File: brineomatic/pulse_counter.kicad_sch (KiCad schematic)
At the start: 6 parts

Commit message: worked on bom for rev b prototype run
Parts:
- C2: LCSC C107149 -> (none)
- R7: LCSC C114526 -> (none)
- R8: LCSC C114561 -> (none)
- R9: LCSC C60816 -> (none)
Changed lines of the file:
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@@
 			)
 		)
-		(property "LCSC" "C60816"
+		(property "LCSC" ""
 			(at 124.46 104.14 0)
 			(effects
@@
 			)
 		)
-		(property "LCSC" "C114526"
+		(property "LCSC" ""
 			(at 111.76 100.33 0)
 			(effects
@@
 			)
 		)
-		(property "LCSC" "C107149"
+		(property "LCSC" ""
 			(at 130.81 107.95 0)
 			(effects
@@
 			)
 		)
-		(property "LCSC" "C114561"
+		(property "LCSC" ""
 			(at 111.76 107.95 0)
 			(effects

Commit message: updated jlc parts rotations and placement offsets
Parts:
- J2: Rotation Offset (none) -> 180
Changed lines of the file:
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@@
+			)
+		)
+		(property "Rotation Offset" "180"
+			(at 100.33 104.14 0)
+			(effects
+				(font
+					(size 1.27 1.27)
+				)
+				(hide yes)
 			)
 		)

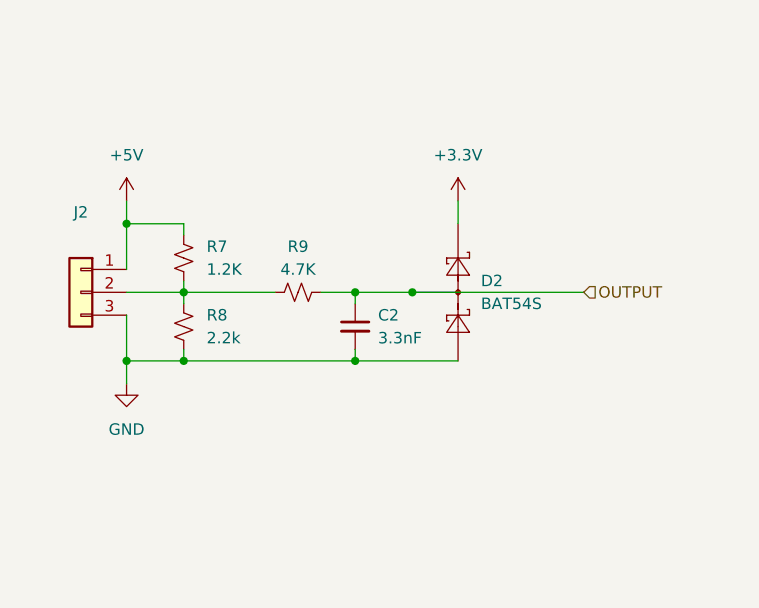
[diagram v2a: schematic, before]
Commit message: added qwiic i2c connector
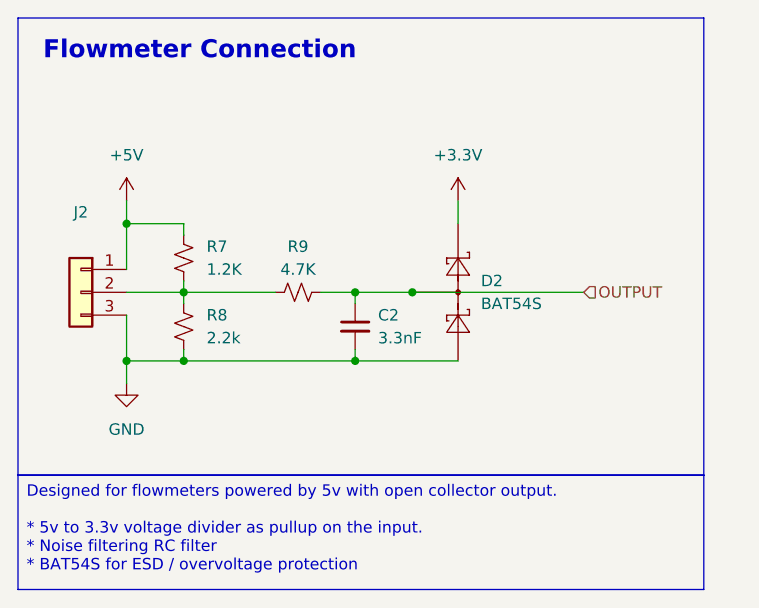
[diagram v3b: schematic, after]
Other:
- note added: "Flowmeter Connection"
- title: (none) -> https://github.com/hoeken/brineomatic
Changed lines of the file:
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@@
 	(generator_version "9.0")
 	(paper "A4")
+	(title_block
+		(title "https://github.com/hoeken/brineomatic")
+		(date "2025-08-28")
+		(rev "B")
+	)
+	(rectangle
+		(start 93.345 73.66)
+		(end 169.545 124.46)
+		(stroke
+			(width 0)
+			(type default)
+		)
+		(fill
+			(type none)
+		)
+	)
+	(text "Flowmeter Connection"
+		(exclude_from_sim no)
+		(at 96.139 77.343 0)
+		(effects
+			(font
+				(size 2 2)
+				(thickness 0.4)
+				(bold yes)
+			)
+			(justify left)
+		)
+	)
+	(text_box "Designed for flowmeters powered by 5v with open collector output.\n\n* 5v to 3.3v voltage divider as pullup on the input.\n* Noise filtering RC filter\n* BAT54S for ESD / overvoltage protection"
+		(exclude_from_sim no)
+		(at 93.345 124.46 0)
+		(size 76.2 12.7)
+		(margins 0.9525 0.9525 0.9525 0.9525)
+		(stroke
+			(width 0)
+			(type solid)
+		)
+		(fill
+			(type none)
+		)
+		(effects
+			(font
+				(size 1.27 1.27)
+			)
+			(justify left top)
+		)
+	)
 	(junction
 		(at 111.76 111.76)

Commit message: added pullup resistor to adc alert
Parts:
- renumbered J2 to J3, R7 to R5, R8 to R6, R9 to R7
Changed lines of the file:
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@@
 		(dnp no)
 		(fields_autoplaced yes)
-		(property "Reference" "#PWR011"
+		(property "Reference" "#PWR013"
 			(at 105.41 120.65 0)
 			(effects
@@
 			(project "brineomatic"
 				(path "/96477ae2-ef08-48f3-8dd4-fe4478541f68/afb25a63-7dc0-4ba4-a0ca-4f0b83c59f3b"
-					(reference "#PWR011")
-					(unit 1)
-				)
-				(path "/96477ae2-ef08-48f3-8dd4-fe4478541f68/c28d9395-3f2f-46b5-bdab-c14b6c7c5c4b"
-					(reference "#PWR031")
+					(reference "#PWR013")
+					(unit 1)
+				)
+				(path "/96477ae2-ef08-48f3-8dd4-fe4478541f68/c28d9395-3f2f-46b5-bdab-c14b6c7c5c4b"
+					(reference "#PWR033")
 					(unit 1)
 				)
@@
 		(dnp no)
 		(fields_autoplaced yes)
-		(property "Reference" "#PWR012"
+		(property "Reference" "#PWR014"
 			(at 142.24 97.79 0)
 			(effects
@@
 			(project "brineomatic"
 				(path "/96477ae2-ef08-48f3-8dd4-fe4478541f68/afb25a63-7dc0-4ba4-a0ca-4f0b83c59f3b"
-					(reference "#PWR012")
-					(unit 1)
-				)
-				(path "/96477ae2-ef08-48f3-8dd4-fe4478541f68/c28d9395-3f2f-46b5-bdab-c14b6c7c5c4b"
-					(reference "#PWR032")
+					(reference "#PWR014")
+					(unit 1)
+				)
+				(path "/96477ae2-ef08-48f3-8dd4-fe4478541f68/c28d9395-3f2f-46b5-bdab-c14b6c7c5c4b"
+					(reference "#PWR034")
 					(unit 1)
 				)
@@
 		(dnp no)
 		(fields_autoplaced yes)
-		(property "Reference" "#PWR010"
+		(property "Reference" "#PWR012"
 			(at 105.41 97.79 0)
 			(effects
@@
 			(project "brineomatic"
 				(path "/96477ae2-ef08-48f3-8dd4-fe4478541f68/afb25a63-7dc0-4ba4-a0ca-4f0b83c59f3b"
-					(reference "#PWR010")
-					(unit 1)
-				)
-				(path "/96477ae2-ef08-48f3-8dd4-fe4478541f68/c28d9395-3f2f-46b5-bdab-c14b6c7c5c4b"
-					(reference "#PWR030")
+					(reference "#PWR012")
+					(unit 1)
+				)
+				(path "/96477ae2-ef08-48f3-8dd4-fe4478541f68/c28d9395-3f2f-46b5-bdab-c14b6c7c5c4b"
+					(reference "#PWR032")
 					(unit 1)
 				)
@@
 		(on_board yes)
 		(dnp no)
-		(property "Reference" "R9"
+		(property "Reference" "R7"
 			(at 124.46 99.06 90)
 			(effects
@@
 			(project "brineomatic"
 				(path "/96477ae2-ef08-48f3-8dd4-fe4478541f68/afb25a63-7dc0-4ba4-a0ca-4f0b83c59f3b"
-					(reference "R9")
+					(reference "R7")
 					(unit 1)
 				)
@@
 		(dnp no)
 		(fields_autoplaced yes)
-		(property "Reference" "J2"
+		(property "Reference" "J3"
 			(at 100.33 95.25 0)
 			(effects
@@
 			(project "brineomatic"
 				(path "/96477ae2-ef08-48f3-8dd4-fe4478541f68/afb25a63-7dc0-4ba4-a0ca-4f0b83c59f3b"
-					(reference "J2")
-					(unit 1)
-				)
-				(path "/96477ae2-ef08-48f3-8dd4-fe4478541f68/c28d9395-3f2f-46b5-bdab-c14b6c7c5c4b"
-					(reference "J10")
+					(reference "J3")
+					(unit 1)
+				)
+				(path "/96477ae2-ef08-48f3-8dd4-fe4478541f68/c28d9395-3f2f-46b5-bdab-c14b6c7c5c4b"
+					(reference "J11")
 					(unit 1)
 				)
@@
 		(dnp no)
 		(fields_autoplaced yes)
-		(property "Reference" "R7"
+		(property "Reference" "R5"
 			(at 114.3 99.0599 0)
 			(effects
@@
 			(project "brineomatic"
 				(path "/96477ae2-ef08-48f3-8dd4-fe4478541f68/afb25a63-7dc0-4ba4-a0ca-4f0b83c59f3b"
-					(reference "R7")
+					(reference "R5")
 					(unit 1)
 				)
@@
 				)
 				(path "/96477ae2-ef08-48f3-8dd4-fe4478541f68/c28d9395-3f2f-46b5-bdab-c14b6c7c5c4b"
-					(reference "C13")
+					(reference "C14")
 					(unit 1)
 				)
@@
 		(dnp no)
 		(fields_autoplaced yes)
-		(property "Reference" "R8"
+		(property "Reference" "R6"
 			(at 114.3 106.6799 0)
 			(effects
@@
 			(project "brineomatic"
 				(path "/96477ae2-ef08-48f3-8dd4-fe4478541f68/afb25a63-7dc0-4ba4-a0ca-4f0b83c59f3b"
-					(reference "R8")
-					(unit 1)
-				)
+					(reference "R6")
+					(unit 1)
+				)

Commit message: 5v power supply is sorted.
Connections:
- net +5V renamed 5V_TRUE
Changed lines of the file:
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@@
+		)
+	)
+	(global_label "5V_TRUE"
+		(shape input)
+		(at 105.41 93.98 90)
+		(fields_autoplaced yes)
+		(effects
+			(font
+				(size 1.27 1.27)
+			)
+			(justify left)
+		)
+		(property "Intersheetrefs" "${INTERSHEET_REFS}"
+			(at 105.41 83.012 90)
+			(effects
+				(font
+					(size 1.27 1.27)
+				)
+				(justify left)
+				(hide yes)
+			)
 		)
 	)
@@
 					(unit 1)
 				)
-			)
-		)
-	)
-	(symbol
-		(lib_id "power:+5V")
-		(at 105.41 93.98 0)
-		(unit 1)
-		(exclude_from_sim no)
-		(in_bom yes)
-		(on_board yes)
-		(dnp no)
-		(fields_autoplaced yes)
-		(property "Reference" "#PWR012"
-			(at 105.41 97.79 0)
-			(effects
-				(font
-					(size 1.27 1.27)
-				)
-				(hide yes)
-			)
-		)
-		(property "Value" "+5V"
-			(at 105.41 88.9 0)
-			(effects
-				(font
-					(size 1.27 1.27)
-				)
-			)
-		)
-		(property "Footprint" ""
-			(at 105.41 93.98 0)
-			(effects
-				(font
-					(size 1.27 1.27)
-				)
-				(hide yes)
-			)
-		)
-		(property "Datasheet" ""
-			(at 105.41 93.98 0)
-			(effects
-				(font
-					(size 1.27 1.27)
-				)
-				(hide yes)
-			)
-		)
-		(property "Description" "Power symbol creates a global label with name \"+5V\""
-			(at 105.41 93.98 0)
-			(effects
-				(font
-					(size 1.27 1.27)
-				)
-				(hide yes)
-			)
-		)
-		(pin "1"
-		)
-		(instances
-			(project "brineomatic"
-				(path "/96477ae2-ef08-48f3-8dd4-fe4478541f68/afb25a63-7dc0-4ba4-a0ca-4f0b83c59f3b"
-					(reference "#PWR012")
-					(unit 1)
-				)
-				(path "/96477ae2-ef08-48f3-8dd4-fe4478541f68/c28d9395-3f2f-46b5-bdab-c14b6c7c5c4b"
-					(reference "#PWR032")
-					(unit 1)
-				)

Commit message: stacked tds, removed stepper vref, pulled in esp32-s3 schematic, added extra relay output
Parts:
- renumbered J3 to J4
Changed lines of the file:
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@@
 		(dnp no)
 		(fields_autoplaced yes)
-		(property "Reference" "#PWR013"
+		(property "Reference" "#PWR014"
 			(at 105.41 120.65 0)
 			(effects
@@
 			(project "brineomatic"
 				(path "/96477ae2-ef08-48f3-8dd4-fe4478541f68/afb25a63-7dc0-4ba4-a0ca-4f0b83c59f3b"
-					(reference "#PWR013")
+					(reference "#PWR014")
 					(unit 1)
 				)
 				(path "/96477ae2-ef08-48f3-8dd4-fe4478541f68/c28d9395-3f2f-46b5-bdab-c14b6c7c5c4b"
-					(reference "#PWR033")
+					(reference "#PWR032")
 					(unit 1)
 				)
@@
 		(dnp no)
 		(fields_autoplaced yes)
-		(property "Reference" "#PWR014"
+		(property "Reference" "#PWR015"
 			(at 142.24 97.79 0)
 			(effects
@@
 			(project "brineomatic"
 				(path "/96477ae2-ef08-48f3-8dd4-fe4478541f68/afb25a63-7dc0-4ba4-a0ca-4f0b83c59f3b"
-					(reference "#PWR014")
+					(reference "#PWR015")
 					(unit 1)
 				)
 				(path "/96477ae2-ef08-48f3-8dd4-fe4478541f68/c28d9395-3f2f-46b5-bdab-c14b6c7c5c4b"
-					(reference "#PWR034")
+					(reference "#PWR033")
 					(unit 1)
 				)
@@
 		(dnp no)
 		(fields_autoplaced yes)
-		(property "Reference" "J3"
+		(property "Reference" "J4"
 			(at 100.33 95.25 0)
 			(effects
@@
 			(project "brineomatic"
 				(path "/96477ae2-ef08-48f3-8dd4-fe4478541f68/afb25a63-7dc0-4ba4-a0ca-4f0b83c59f3b"
-					(reference "J3")
-					(unit 1)
-				)
+					(reference "J4")
+					(unit 1)
+				)

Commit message: all connectors are now flush withe 3mm outside edge of the case
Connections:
- net 5V_TRUE renamed +5V
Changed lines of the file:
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@@
-		)
-	)
-	(global_label "5V_TRUE"
-		(shape input)
-		(at 105.41 93.98 90)
-		(fields_autoplaced yes)
-		(effects
-			(font
-				(size 1.27 1.27)
-			)
-			(justify left)
-		)
-		(property "Intersheetrefs" "${INTERSHEET_REFS}"
-			(at 105.41 83.012 90)
-			(effects
-				(font
-					(size 1.27 1.27)
-				)
-				(justify left)
-				(hide yes)
-			)
 		)
 	)
@@
 				)
 				(path "/96477ae2-ef08-48f3-8dd4-fe4478541f68/c28d9395-3f2f-46b5-bdab-c14b6c7c5c4b"
-					(reference "D13")
-					(unit 1)
-				)
+					(reference "D12")
+					(unit 1)
+				)
+			)
+		)
+	)
+	(symbol
+		(lib_id "power:+5V")
+		(at 105.41 93.98 0)
+		(unit 1)
+		(exclude_from_sim no)
+		(in_bom yes)
+		(on_board yes)
+		(dnp no)
+		(fields_autoplaced yes)
+		(property "Reference" "#PWR069"
+			(at 105.41 97.79 0)
+			(effects
+				(font
+					(size 1.27 1.27)
+				)
+				(hide yes)
+			)
+		)
+		(property "Value" "+5V"
+			(at 105.41 88.9 0)
+			(effects
+				(font
+					(size 1.27 1.27)
+				)
+			)
+		)
+		(property "Footprint" ""
+			(at 105.41 93.98 0)
+			(effects
+				(font
+					(size 1.27 1.27)
+				)
+				(hide yes)
+			)
+		)
+		(property "Datasheet" ""
+			(at 105.41 93.98 0)
+			(effects
+				(font
+					(size 1.27 1.27)
+				)
+				(hide yes)
+			)
+		)
+		(property "Description" "Power symbol creates a global label with name \"+5V\""
+			(at 105.41 93.98 0)
+			(effects
+				(font
+					(size 1.27 1.27)
+				)
+				(hide yes)
+			)
+		)
+		(pin "1"
+		)
+		(instances
+			(project ""
+				(path "/96477ae2-ef08-48f3-8dd4-fe4478541f68/afb25a63-7dc0-4ba4-a0ca-4f0b83c59f3b"
+					(reference "#PWR069")
+					(unit 1)
+				)
+				(path "/96477ae2-ef08-48f3-8dd4-fe4478541f68/c28d9395-3f2f-46b5-bdab-c14b6c7c5c4b"
+					(reference "#PWR070")
+					(unit 1)
+				)
